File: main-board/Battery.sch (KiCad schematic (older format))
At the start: 2 parts

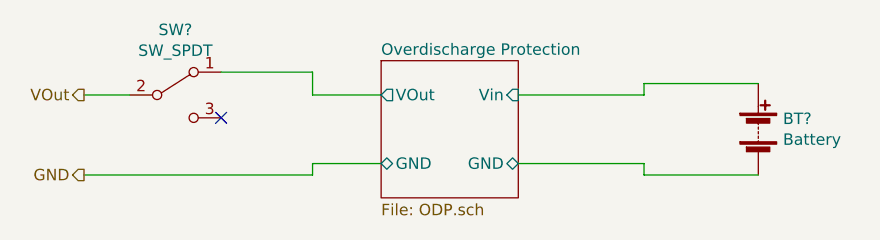
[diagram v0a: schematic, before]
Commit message: removed battery protection (will be implemented off-board)
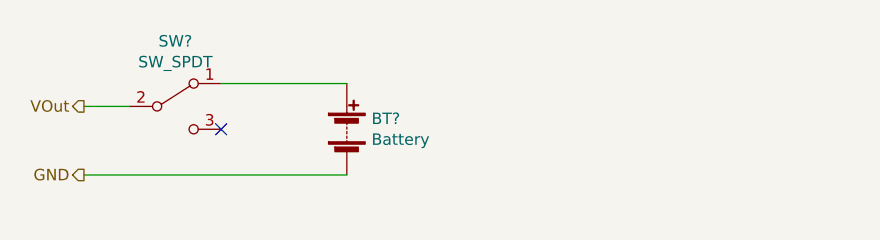
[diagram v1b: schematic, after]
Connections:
- net Overdischarge Protection/GND is gone; now on net GND: BT?.2 (-)
- net Overdischarge Protection/Vin is gone; now on an unnamed net: BT?.1 (+)
- net Overdischarge Protection/VOut: no longer names the net of SW?.1 (A)
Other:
- moved on the sheet: BT?, SW?
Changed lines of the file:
@@
 Comment4 ""
 $EndDescr
-Text HLabel 3000 2500 0    50   Output ~ 0
+Text HLabel 3000 2550 0    50   Output ~ 0
 VOut
 Text HLabel 3000 2850 0    50   Output ~ 0
 GND
-$Sheet
-S 4300 2350 600  600
-U 60751DD3
-F0 "Overdischarge Protection" 50
-F1 "ODP.sch" 50
-F2 "VOut" O L 4300 2500 50
-F3 "Vin" I R 4900 2500 50
-F4 "GND" B R 4900 2800 50
-F5 "GND" B L 4300 2800 50
-$EndSheet
 $Comp
 L Switch:SW_SPDT SW?
 U 1 1 607522AC
-P 3400 2500
-F 0 "SW?" H 3400 2785 50  0000 C CNN
-F 1 "SW_SPDT" H 3400 2694 50  0000 C CNN
-F 2 "" H 3400 2500 50  0001 C CNN
-F 3 "~" H 3400 2500 50  0001 C CNN
-	1    3400 2500
+P 3400 2550
+F 0 "SW?" H 3400 2835 50  0000 C CNN
+F 1 "SW_SPDT" H 3400 2744 50  0000 C CNN
+F 2 "" H 3400 2550 50  0001 C CNN
+F 3 "~" H 3400 2550 50  0001 C CNN
+	1    3400 2550
 	1    0    0    -1
 $EndComp
@@
 L Device:Battery BT?
 U 1 1 60752A0B
-P 5950 2650
-F 0 "BT?" H 6058 2696 50  0000 L CNN
-F 1 "Battery" H 6058 2605 50  0000 L CNN
-F 2 "" V 5950 2710 50  0001 C CNN
-F 3 "~" V 5950 2710 50  0001 C CNN
-	1    5950 2650
+P 4150 2650
+F 0 "BT?" H 4258 2696 50  0000 L CNN
+F 1 "Battery" H 4258 2605 50  0000 L CNN
+F 2 "" V 4150 2710 50  0001 C CNN
+F 3 "~" V 4150 2710 50  0001 C CNN
+	1    4150 2650
 	1    0    0    -1
 $EndComp
 Wire Wire Line
-	5950 2850 5450 2850
+	3000 2550 3200 2550
+NoConn ~ 3600 2650
 Wire Wire Line
-	5450 2850 5450 2800
+	3000 2850 4150 2850
 Wire Wire Line
-	5450 2800 4900 2800
-Wire Wire Line
-	4900 2500 5450 2500
-Wire Wire Line
-	5450 2500 5450 2450
-Wire Wire Line
-	5450 2450 5950 2450
-Wire Wire Line
-	4300 2500 4000 2500
-Wire Wire Line
-	4000 2500 4000 2400
-Wire Wire Line
-	4000 2400 3600 2400
-Wire Wire Line
-	3000 2500 3200 2500
-Wire Wire Line
-	3000 2850 4000 2850
-Wire Wire Line
-	4000 2850 4000 2800
-Wire Wire Line
-	4000 2800 4300 2800
-NoConn ~ 3600 2600
+	3600 2450 4150 2450
 $EndSCHEMATC
